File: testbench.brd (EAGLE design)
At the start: 100 x 100 mm, 40 parts, among them T1 C8492, T2 C8492, T3 C8545, T4 C8545, X1 MKDSN1,5/2-5,08

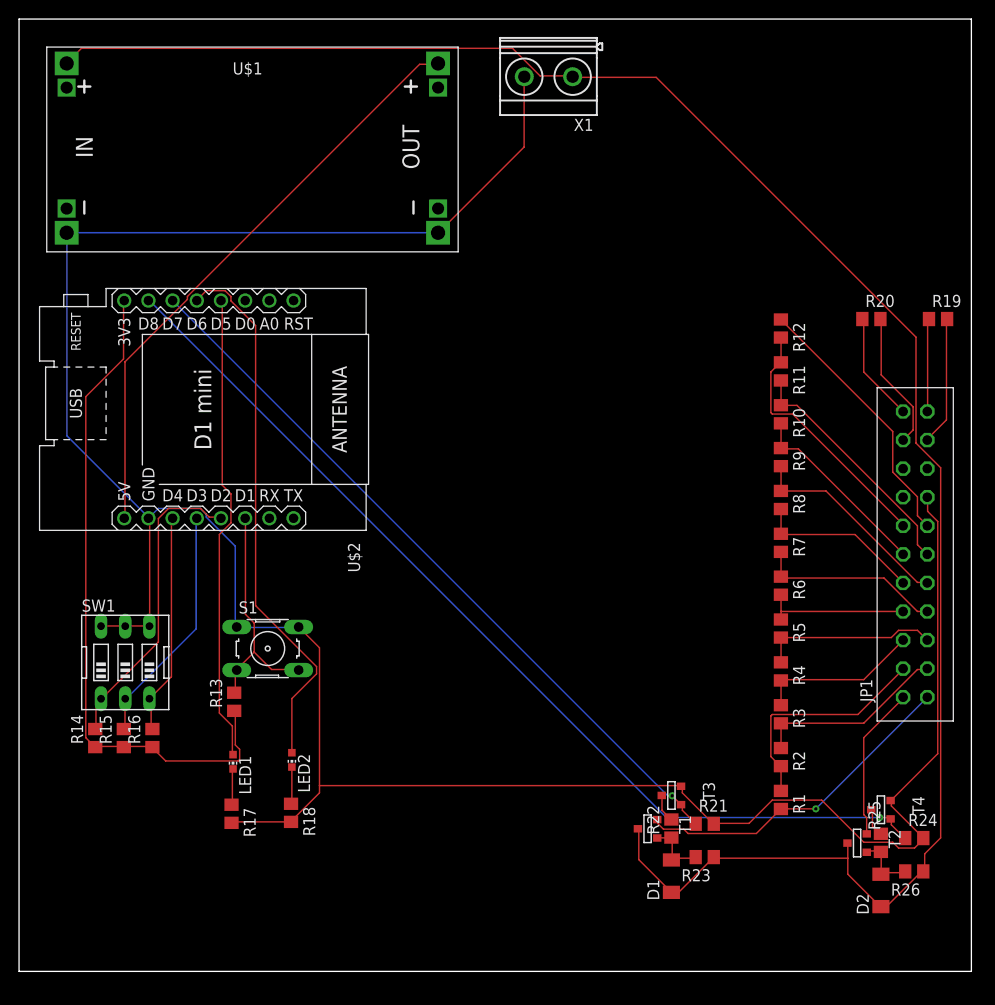
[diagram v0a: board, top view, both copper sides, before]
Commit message: routing and placement updated, dimensions changed
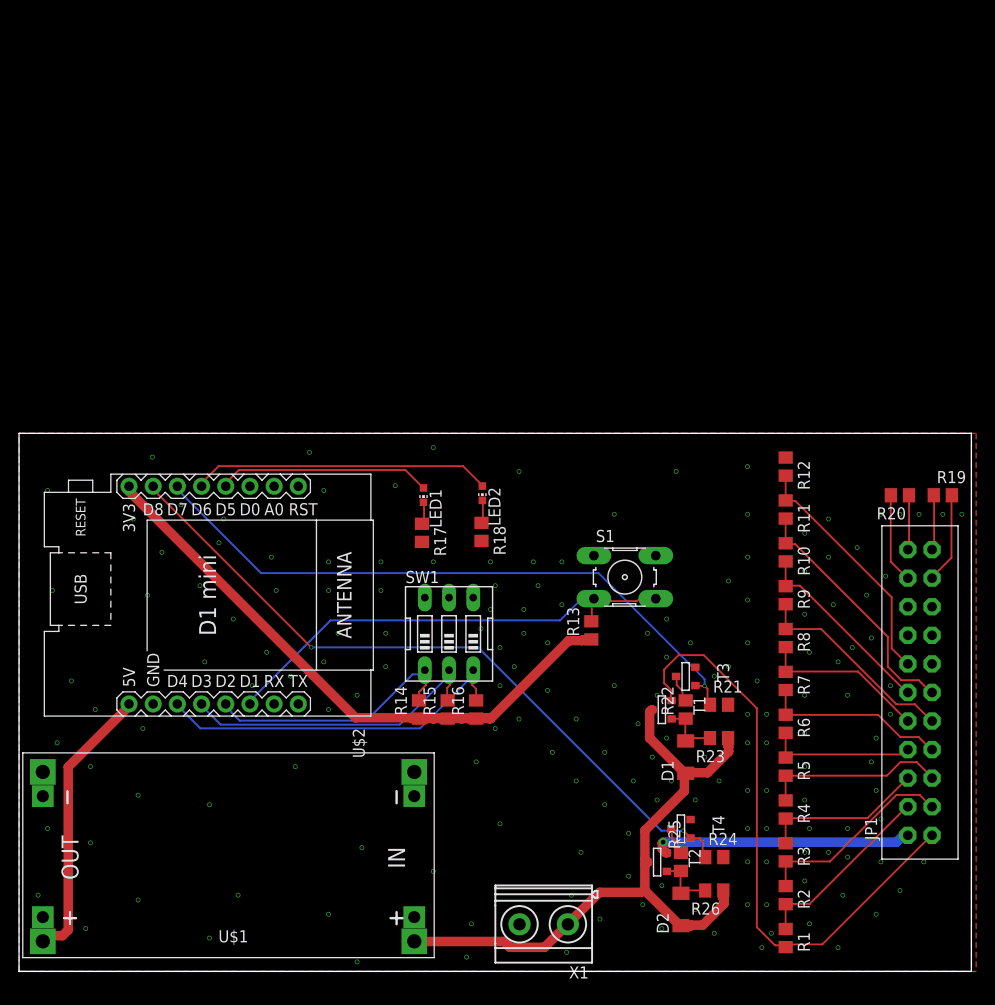
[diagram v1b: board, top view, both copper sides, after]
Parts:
- moved X1 89.0 mm to (55.1, 4.97)
- moved U$1 67.4 mm to (41.5, 20.9), turned to 180 degrees
- moved R13 38.2 mm to (60.1, 35.8)
- moved S1 38.2 mm to (63.6, 41.4)
- moved R17 35.6 mm to (42.3, 46.0)
- moved R18 35.6 mm to (48.6, 46.1)
- moved LED1 34.4 mm to (42.5, 50.0)
- moved LED2 34.4 mm to (48.6, 50.2)
- moved R14 34.1 mm to (42.0, 27.5)
- moved R15 34.1 mm to (45.0, 27.5)
- moved R16 34.1 mm to (48.0, 27.5)
- moved SW1 34.1 mm to (45.1, 35.4)
- moved D2 21.1 mm to (69.5, 6.50)
- moved R24 21.1 mm to (73.0, 12.0)
- moved R25 21.1 mm to (69.5, 11.5)
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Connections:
- removed net N$18: JP1.9, R12.1
- net GND: now also JP1.9, R12.1
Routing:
- net GND: track 273.3 -> 0.00 mm, vias 0 -> 172
- net 48VDC: track 202.9 -> 68.9 mm
- net +5V: track 62.5 -> 29.5 mm
- net BATSIM: track 35.1 -> 63.4 mm, vias 1 -> 0
- net D8: track 103.2 -> 75.2 mm, vias 1 -> 2
- net N$18: track 28.0 -> 0.00 mm
- net N$21: track 49.3 -> 22.5 mm
- net N$20: track 57.0 -> 31.5 mm
- net N$12: track 25.1 -> 50.1 mm
- net N$15: track 23.4 -> 38.5 mm
- net N$19: track 16.2 -> 27.4 mm, vias 0 -> 1
- net D7: track 78.0 -> 67.9 mm
- net N$14: track 25.4 -> 33.1 mm
- net +3V3: track 70.3 -> 62.9 mm
- net THERMO2_IN: track 11.5 -> 5.83 mm
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- added copper zone on layer 1, net GND
- added copper zone on layer 16, net GND
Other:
- board size 100 x 100 mm -> 100 x 56.5 mm

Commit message: display added
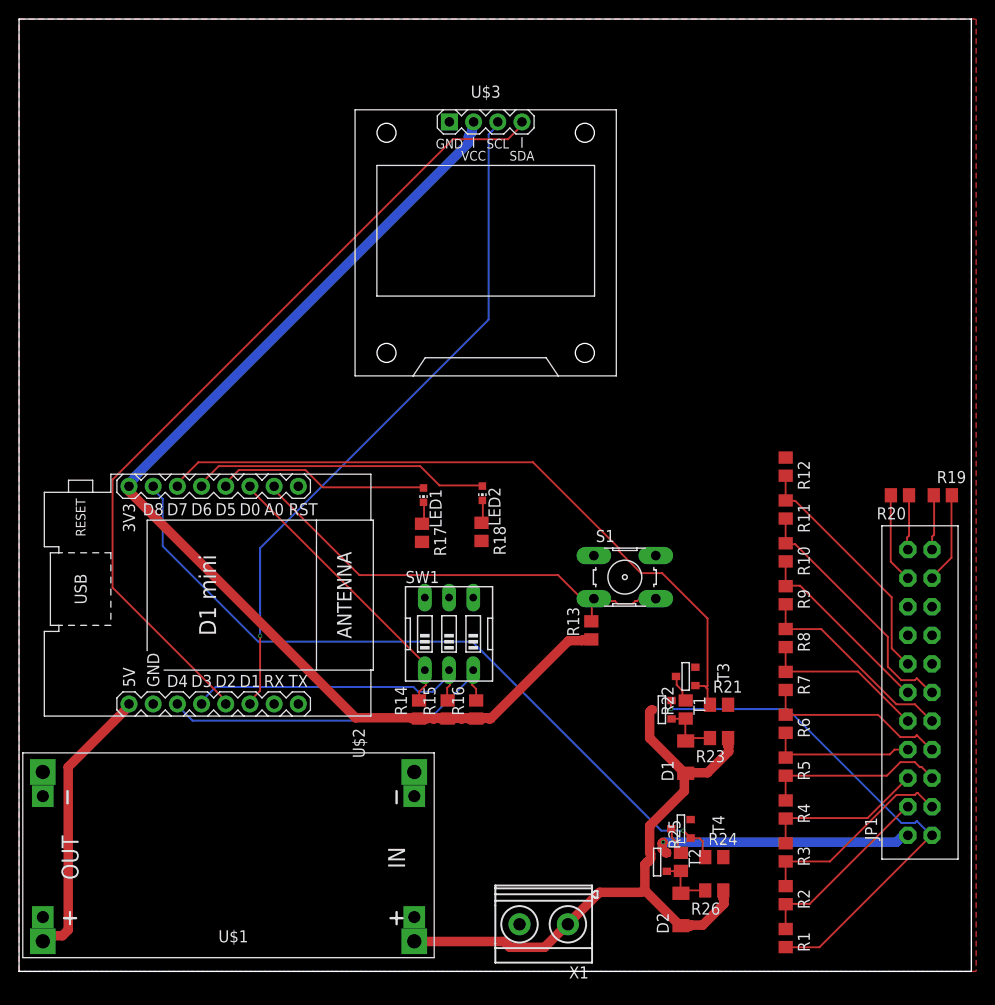
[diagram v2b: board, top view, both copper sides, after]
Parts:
- added U$3: DISPLAY-OLED-128X64-I2C, diy-modules:DISPLAY-OLED-128X64-I2C
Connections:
- removed net N$12: R13.2, S1.3, S1.4, U$2.JP2.3
- removed net N$13: R14.2, SW1.1, U$2.JP2.4
- new net A0: R13.2, S1.3, S1.4, U$2.JP1.2
- new net D0: R14.2, SW1.1, U$2.JP1.3
- new net D1: U$2.JP2.3, U$3.3
- new net D2: U$2.JP2.4, U$3.4
- net +3V3: now also U$3.2
- net GND: now also U$3.1
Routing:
- net D2: track 0.00 -> 87.2 mm
- net D1: track 0.00 -> 71.9 mm, vias 0 -> 1
- net +3V3: track 62.9 -> 116.1 mm
- net N$12: track 50.1 -> 0.00 mm
- net A0: track 0.00 -> 48.3 mm
- net D0: track 0.00 -> 30.5 mm
- net N$13: track 27.5 -> 0.00 mm
- net BATSIM: track 63.4 -> 54.3 mm, vias 0 -> 1
- net D7: track 67.9 -> 74.4 mm, vias 1 -> 0
- net D8: track 75.2 -> 78.1 mm, vias 2 -> 1
- net N$14: track 33.1 -> 31.8 mm
- net N$15: track 38.5 -> 37.8 mm
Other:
- board size 100 x 56.5 mm -> 100 x 100 mm

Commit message: routing updated
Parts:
- added H1, H2, H3, H4: MOUNT-PAD-ROUND3.2, holes:3,2-PAD
- moved U$1 8.50 mm to (50.0, 20.9)
- moved X1 4.50 mm to (59.6, 4.97)
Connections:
- net GND: now also H1.B3,2, H2.B3,2, H3.B3,2, H4.B3,2
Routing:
- net D2: track 87.2 -> 75.3 mm, vias 0 -> 2
- net 48VDC: track 68.7 -> 60.1 mm
- net D7: track 74.4 -> 77.7 mm
- net +5V: track 29.5 -> 27.7 mm
- net D8: track 78.1 -> 79.5 mm
